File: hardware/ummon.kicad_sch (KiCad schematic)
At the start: 84 parts, among them J1 Conn_01x08_Pin, J2 Conn_01x05_Pin, J3 Conn_01x04_Pin, J4 Conn_01x04_Pin, J5 Conn_01x04_Pin, P1 FPC 0.5MM 24P Vertical, Q1 SI1308EDL, SW1 Reboot, SW2 Flash, SW3 Test Button, U1 ESP32-C6-WROOM-1-N8, U2 SCD41-D-R2, U3 SGP41-D-R4, U4 SHT41-AD1B-R2, U5 AMS1117-3.3

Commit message: :sparkles: Add various testpoints
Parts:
- added TP1, TP10, TP2, TP3, TP4, TP5, TP6, TP7, TP8, TP9: TestPoint, TestPoint:TestPoint_Pad_D1.0mm, symbol Connector:TestPoint
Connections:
- net +3.3V: now also TP10.1
- net +5V: now also TP8.1
- net EN: now also TP1.1
- net EPD_PREVGH: now also TP4.1
- net EPD_PREVGL: now also TP5.1
- net EPD_RESE: now also TP3.1
- net GND: now also TP9.1
- net GPIO9: now also TP2.1
- net EPD_VGL: now reaches C26.1, D3.2 (A), D4.1 (K)
- net EPD_VGL: now also TP6.1
- net EPD_VGH: now reaches C26.2, D2.2 (A), L1.2, Q1.3 (D)
- net EPD_VGH: now also TP7.1

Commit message: :construction: WIP buck converter
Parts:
- added L2: FTC252012S2R2MBCA, parts:IND-SMD_L2.5-W2.0_MHCHL2520, symbol parts:FTC252012S2R2MBCA
- added R17: 100kΩ, Resistor_SMD:R_0805_2012Metric, symbol Device:R_Small
- added R18: 49.9kΩ, Resistor_SMD:R_0805_2012Metric, symbol Device:R_Small
- added U6: TLV62569DBVR, parts:SOT-23-5_L3.0-W1.7-P0.95-LS2.8-BR, symbol parts:TLV62569DBVR
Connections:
- net +3.3V: now also R17.2, R18.1, U6.5 (FB); no longer C16.1, U5.4 (VOUT)
- net +5V: now also U6.1 (EN)
- net GND: now also R18.2, U6.2 (GND)
- new net: L2.1, U6.3 (SW)
- new net: L2.2, R17.1
- new net: C16.1, U5.4 (VOUT)
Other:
- moved on the sheet: C14, C15, C16, C17, LED1, R14, U5

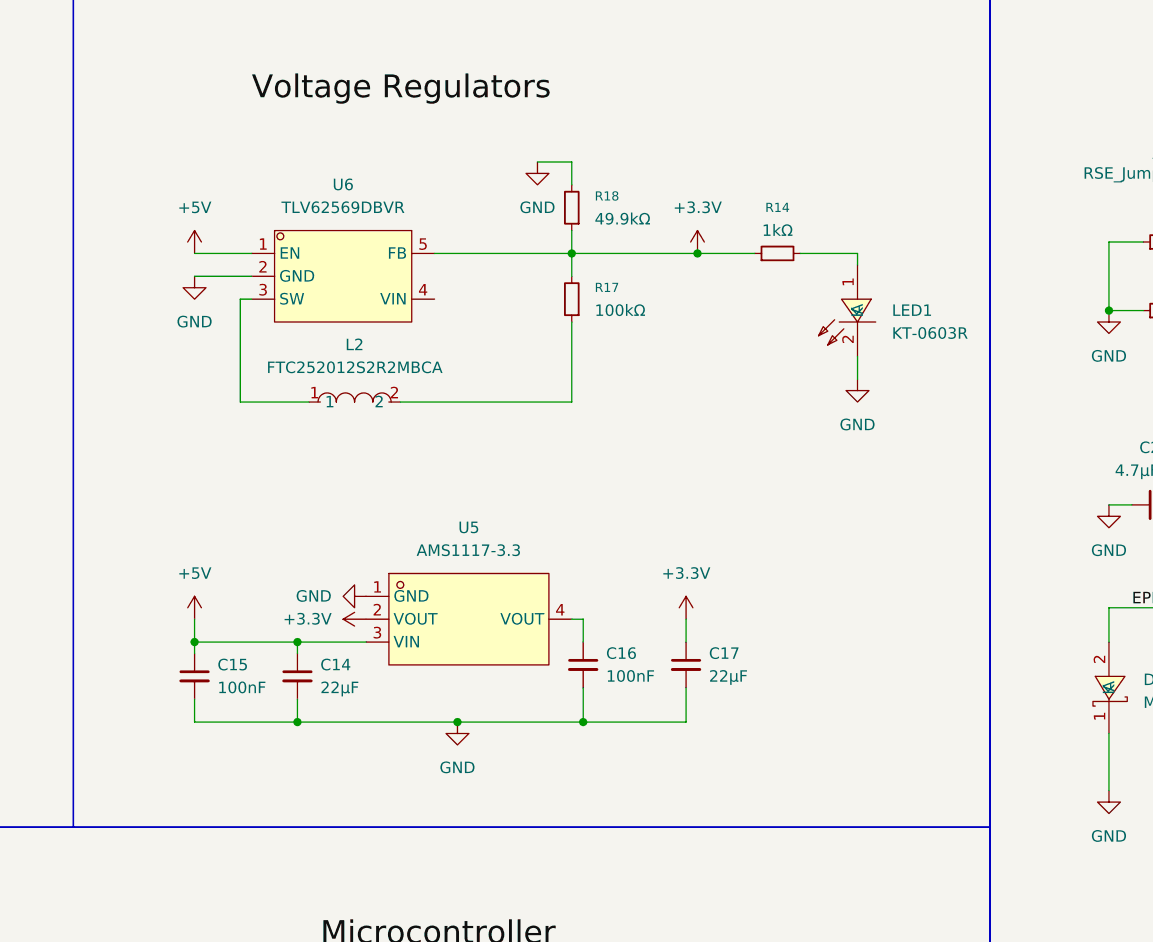
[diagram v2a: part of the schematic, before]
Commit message: Revert ":construction: WIP buck converter"
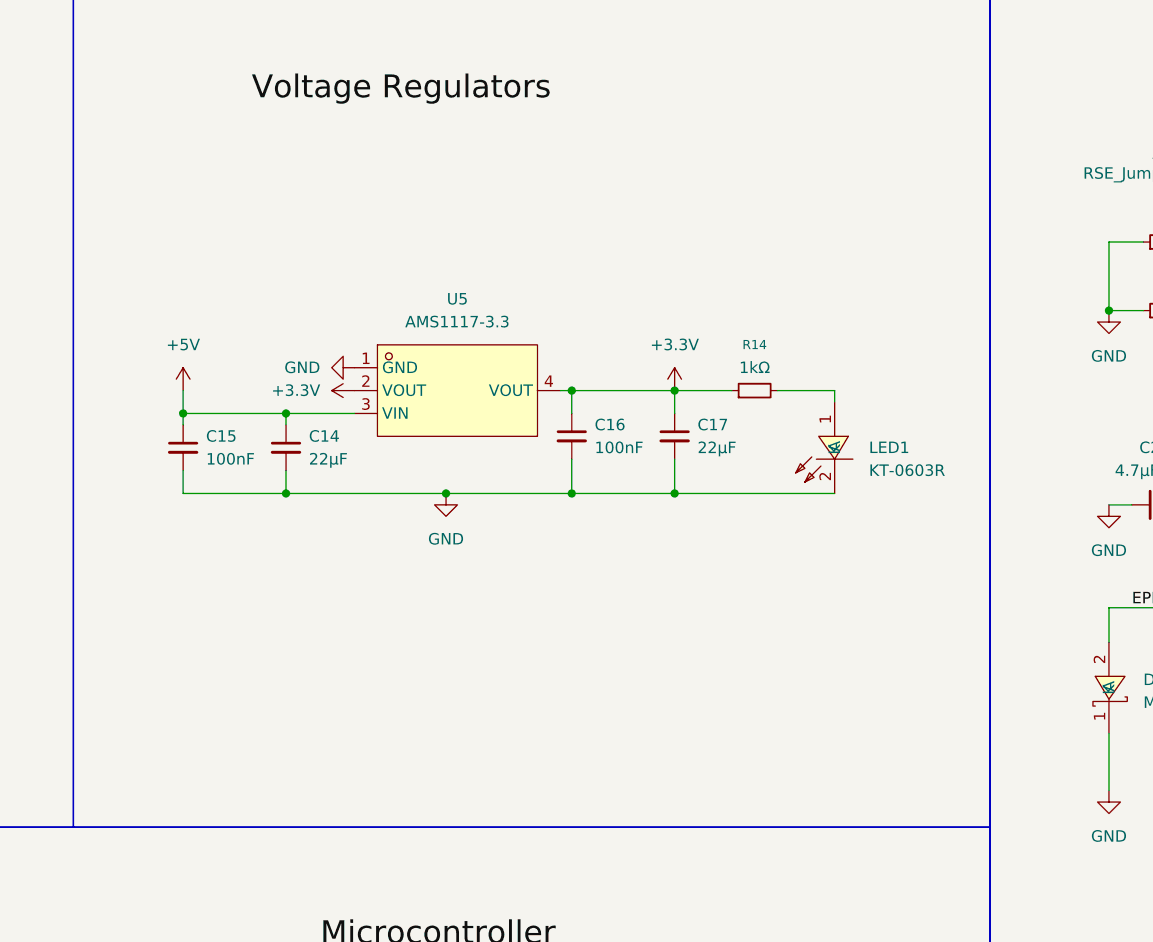
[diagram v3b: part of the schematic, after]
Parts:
- removed L2: FTC252012S2R2MBCA, parts:IND-SMD_L2.5-W2.0_MHCHL2520, symbol parts:FTC252012S2R2MBCA
- removed R17: 100kΩ, Resistor_SMD:R_0805_2012Metric, symbol Device:R_Small
- removed R18: 49.9kΩ, Resistor_SMD:R_0805_2012Metric, symbol Device:R_Small
- removed U6: TLV62569DBVR, parts:SOT-23-5_L3.0-W1.7-P0.95-LS2.8-BR, symbol parts:TLV62569DBVR
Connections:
- net +3.3V: now also C16.1, U5.4 (VOUT)
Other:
- moved on the sheet: C14, C15, C16, C17, LED1, R14, U5

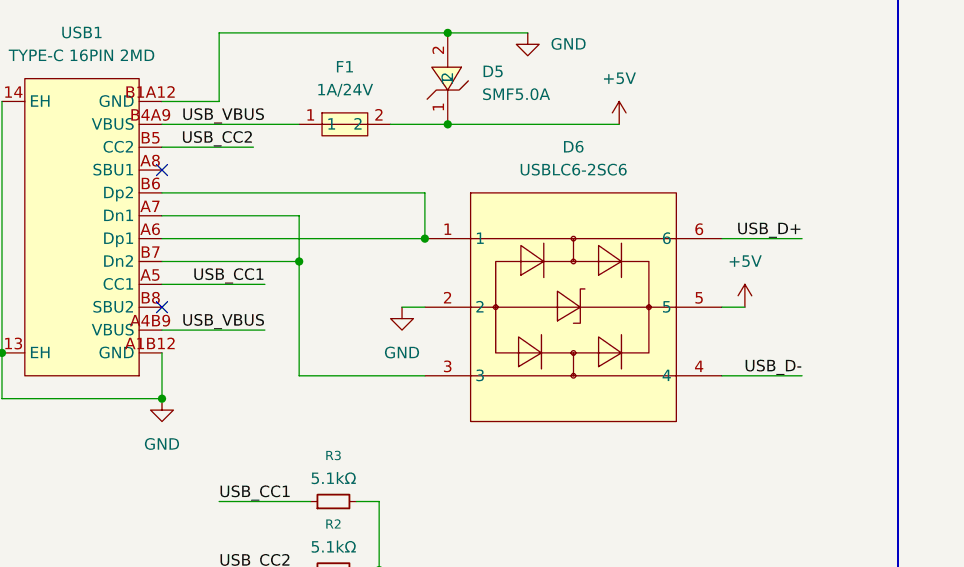
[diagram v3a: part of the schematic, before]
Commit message: :recycle: Swap USB data lines between USBLC6 channels
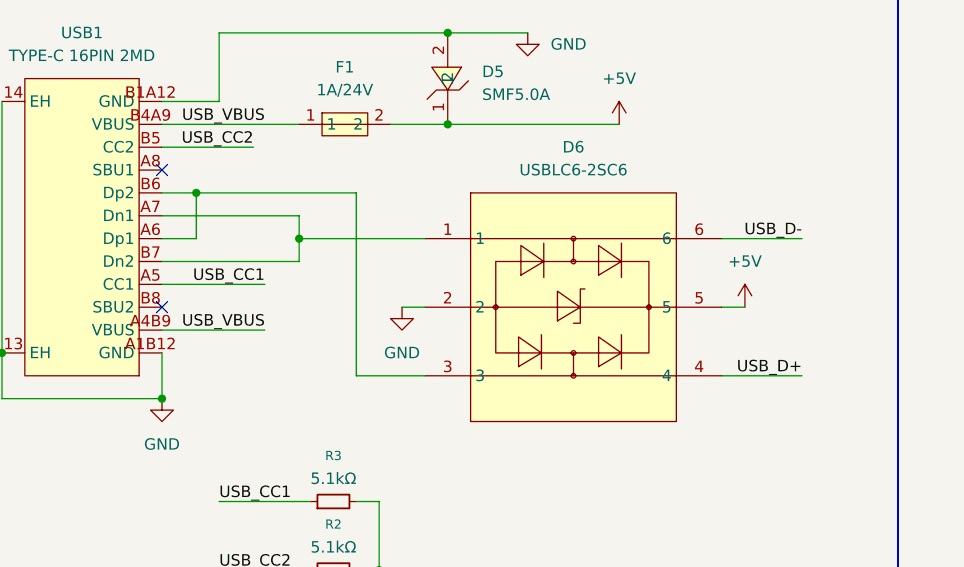
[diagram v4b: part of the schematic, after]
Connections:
- net USB_D+: now also D6.4; no longer D6.6
- net USB_D-: now also D6.6; no longer D6.4
- net at USB1.A6 (Dp1), USB1.B6 (Dp2): now also D6.3; no longer D6.1
- net at USB1.A7 (Dn1), USB1.B7 (Dn2): now also D6.1; no longer D6.3
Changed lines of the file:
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@@
 	)
 	(junction
-		(at 66.04 54.61)
+		(at 40.64 49.53)
 		(diameter 0)
 		(color 0 0 0 0)
@@
 	)
 	(junction
-		(at 52.07 57.15)
-		(diameter 0)
-		(color 0 0 0 0)
-	)
-	(junction
 		(at 364.49 83.82)
 		(diameter 0)
@@
 	)
 	(junction
+		(at 52.07 54.61)
+		(diameter 0)
+		(color 0 0 0 0)
+	)
+	(junction
 		(at 67.31 152.4)
 		(diameter 0)
@@
 	(wire
 		(pts
-			(xy 52.07 57.15) (xy 52.07 52.07)
+			(xy 52.07 57.15) (xy 52.07 54.61)
 		)
 		(stroke
@@
 	(wire
 		(pts
+			(xy 40.64 54.61) (xy 40.64 49.53)
+		)
+		(stroke
+			(width 0)
+			(type default)
+		)
+	)
+	(wire
+		(pts
 			(xy 227.33 248.92) (xy 227.33 255.27)
 		)
@@
 	(wire
 		(pts
-			(xy 203.2 55.88) (xy 203.2 57.15)
+			(xy 52.07 54.61) (xy 52.07 52.07)
 		)
 		(stroke
@@
 	(wire
 		(pts
-			(xy 134.62 134.62) (xy 134.62 133.35)
+			(xy 203.2 55.88) (xy 203.2 57.15)
 		)
 		(stroke
@@
 	(wire
 		(pts
-			(xy 227.33 243.84) (xy 227.33 237.49)
+			(xy 134.62 134.62) (xy 134.62 133.35)
 		)
 		(stroke
@@
 	(wire
 		(pts
-			(xy 17.78 173.99) (xy 24.13 173.99)
+			(xy 227.33 243.84) (xy 227.33 237.49)
 		)
 		(stroke
@@
 	(wire
 		(pts
-			(xy 247.65 237.49) (xy 271.78 237.49)
+			(xy 17.78 173.99) (xy 24.13 173.99)
 		)
 		(stroke
@@
 	(wire
 		(pts
-			(xy 270.51 80.01) (xy 270.51 83.82)
+			(xy 247.65 237.49) (xy 271.78 237.49)
 		)
 		(stroke
@@
 	(wire
 		(pts
-			(xy 66.04 49.53) (xy 66.04 54.61)
+			(xy 270.51 80.01) (xy 270.51 83.82)
 		)
 		(stroke
@@
 	(wire
 		(pts
-			(xy 52.07 69.85) (xy 66.04 69.85)
-		)
-		(stroke
-			(width 0)
-			(type default)
-		)
-	)
-	(wire
-		(pts
 			(xy 370.84 40.64) (xy 382.27 40.64)
 		)
@@
 	(wire
 		(pts
-			(xy 365.76 67.31) (xy 365.76 71.12)
+			(xy 36.83 54.61) (xy 40.64 54.61)
 		)
 		(stroke
@@
 	(wire
 		(pts
-			(xy 22.86 137.16) (xy 29.21 137.16)
+			(xy 365.76 67.31) (xy 365.76 71.12)
 		)
 		(stroke
@@
 	(wire
 		(pts
-			(xy 248.92 107.95) (xy 251.46 107.95)
+			(xy 22.86 137.16) (xy 29.21 137.16)
 		)
 		(stroke
@@
 	(wire
 		(pts
-			(xy 173.99 55.88) (xy 172.72 55.88)
+			(xy 248.92 107.95) (xy 251.46 107.95)
 		)
 		(stroke
@@
 	(wire
 		(pts
-			(xy 138.43 166.37) (xy 133.35 166.37)
+			(xy 173.99 55.88) (xy 172.72 55.88)
 		)
 		(stroke
@@
 	(wire
 		(pts
-			(xy 196.85 55.88) (xy 203.2 55.88)
+			(xy 138.43 166.37) (xy 133.35 166.37)
 		)
 		(stroke
@@
 	(wire
 		(pts
-			(xy 36.83 49.53) (xy 66.04 49.53)
+			(xy 196.85 55.88) (xy 203.2 55.88)
 		)
 		(stroke
@@
 	(wire
 		(pts
+			(xy 58.42 69.85) (xy 66.04 69.85)
+		)
+		(stroke
+			(width 0)
+			(type default)
+		)
+	)
+	(wire
+		(pts
 			(xy 207.01 237.49) (xy 213.36 237.49)
 		)
@@
 	(wire
 		(pts
+			(xy 40.64 49.53) (xy 58.42 49.53)
+		)
+		(stroke
+			(width 0)
+			(type default)
+		)
+	)
+	(wire
+		(pts
 			(xy 46.99 173.99) (xy 35.56 173.99)
 		)
@@
 	(wire
 		(pts
+			(xy 52.07 54.61) (xy 66.04 54.61)
+		)
+		(stroke
+			(width 0)
+			(type default)
+		)
+	)
+	(wire
+		(pts
 			(xy 68.58 41.91) (xy 87.63 41.91)
 		)
@@
 	(wire
 		(pts
-			(xy 36.83 54.61) (xy 66.04 54.61)
-		)
-		(stroke
-			(width 0)
-			(type default)
-		)
-	)
-	(wire
-		(pts
 			(xy 130.81 59.69) (xy 130.81 58.42)
 		)
@@
 	(wire
 		(pts
+			(xy 58.42 49.53) (xy 58.42 69.85)
+		)
+		(stroke
+			(width 0)
+			(type default)
+		)
+	)
+	(wire
+		(pts
 			(xy 247.65 259.08) (xy 251.46 259.08)
 		)
@@
 	(wire
 		(pts
+			(xy 36.83 49.53) (xy 40.64 49.53)
+		)
+		(stroke
+			(width 0)
+			(type default)
+		)
+	)
+	(wire
+		(pts
 			(xy 353.06 93.98) (xy 382.27 93.98)
 		)
@@
 	(wire
 		(pts
-			(xy 52.07 57.15) (xy 52.07 69.85)
-		)
-		(stroke
-			(width 0)
-			(type default)
-		)
-	)
-	(wire
-		(pts
 			(xy 149.86 240.03) (xy 149.86 241.3)
 		)
@@
 		)
 	)
-	(label "USB_D+"
-		(at 107.95 54.61 180)
-		(effects
-			(font
-				(size 1.27 1.27)
-			)
-			(justify right bottom)
-		)
-	)
 	(label "I2C_SCL"
 		(at 389.89 185.42 180)
@@
 	)
 	(label "USB_D+"
+		(at 107.95 69.85 180)
+		(effects
+			(font
+				(size 1.27 1.27)
+			)
+			(justify right bottom)
+		)
+	)
+	(label "USB_D+"
 		(at 133.35 171.45 180)
 		(effects
@@
 		)
 	)
-	(label "USB_D-"
-		(at 107.95 69.85 180)
-		(effects
-			(font
-				(size 1.27 1.27)
-			)
-			(justify right bottom)
-		)
-	)
 	(label "USB_CC2"
 		(at 43.18 91.44 0)
@@
 		)
 	)
+	(label "USB_D-"
+		(at 107.95 54.61 180)
+		(effects
+			(font
+				(size 1.27 1.27)
+			)
+			(justify right bottom)
+		)
+	)

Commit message: :construction: WIP place ESD parts and route epd charge pump
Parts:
- added C18: 22µF, Capacitor_SMD:C_1206_3216Metric, symbol Device:C_Small
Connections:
- net +3.3V: now also C18.2
- net GND: now also C18.1
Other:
- moved on the sheet: C22
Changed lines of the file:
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@@
 	)
 	(junction
+		(at 229.87 46.99)
+		(diameter 0)
+		(color 0 0 0 0)
+	)
+	(junction
 		(at 149.86 247.65)
 		(diameter 0)
@@
 	)
 	(junction
+		(at 229.87 68.58)
+		(diameter 0)
+		(color 0 0 0 0)
+	)
+	(junction
 		(at 160.02 133.35)
 		(diameter 0)
@@
 	)
 	(junction
-		(at 233.68 46.99)
-		(diameter 0)
-		(color 0 0 0 0)
-	)
-	(junction
 		(at 342.9 93.98)
 		(diameter 0)
@@
 	)
 	(junction
+		(at 242.57 68.58)
+		(diameter 0)
+		(color 0 0 0 0)
+	)
+	(junction
 		(at 217.17 237.49)
 		(diameter 0)
@@
 	(wire
 		(pts
+			(xy 238.76 58.42) (xy 242.57 58.42)
+		)
+		(stroke
+			(width 0)
+			(type default)
+		)
+	)
+	(wire
+		(pts
 			(xy 342.9 86.36) (xy 342.9 88.9)
 		)
@@
 	(wire
 		(pts
+			(xy 229.87 68.58) (xy 233.68 68.58)
+		)
+		(stroke
+			(width 0)
+			(type default)
+		)
+	)
+	(wire
+		(pts
 			(xy 60.96 142.24) (xy 60.96 152.4)
 		)
@@
 	(wire
 		(pts
+			(xy 242.57 58.42) (xy 242.57 68.58)
+		)
+		(stroke
+			(width 0)
+			(type default)
+		)
+	)
+	(wire
+		(pts
 			(xy 342.9 93.98) (xy 342.9 97.79)
 		)
@@
 	(wire
 		(pts
-			(xy 233.68 46.99) (xy 237.49 46.99)
-		)
-		(stroke
-			(width 0)
-			(type default)
-		)
-	)
-	(wire
-		(pts
 			(xy 270.51 62.23) (xy 270.51 64.77)
 		)
@@
 	(wire
 		(pts
-			(xy 237.49 39.37) (xy 233.68 39.37)
+			(xy 237.49 39.37) (xy 229.87 39.37)
 		)
 		(stroke
@@
 	(wire
 		(pts
+			(xy 229.87 46.99) (xy 237.49 46.99)
+		)
+		(stroke
+			(width 0)
+			(type default)
+		)
+	)
+	(wire
+		(pts
 			(xy 146.05 247.65) (xy 149.86 247.65)
 		)
@@
 	(wire
 		(pts
+			(xy 229.87 58.42) (xy 229.87 68.58)
+		)
+		(stroke
+			(width 0)
+			(type default)
+		)
+	)
+	(wire
+		(pts
 			(xy 217.17 248.92) (xy 224.79 248.92)
 		)
@@
 	(wire
 		(pts
+			(xy 242.57 68.58) (xy 246.38 68.58)
+		)
+		(stroke
+			(width 0)
+			(type default)
+		)
+	)
+	(wire
+		(pts
 			(xy 39.37 255.27) (xy 52.07 255.27)
 		)
@@
 	(wire
 		(pts
-			(xy 241.3 68.58) (xy 246.38 68.58)
+			(xy 238.76 68.58) (xy 242.57 68.58)
 		)
 		(stroke
@@
 	(wire
 		(pts
-			(xy 233.68 39.37) (xy 233.68 46.99)
+			(xy 229.87 39.37) (xy 229.87 46.99)
 		)
 		(stroke
@@
 	(wire
 		(pts
-			(xy 233.68 68.58) (xy 236.22 68.58)
-		)
-		(stroke
-			(width 0)
-			(type default)
-		)
-	)
-	(wire
-		(pts
 			(xy 67.31 130.81) (xy 78.74 130.81)
 		)
@@
 	(wire
 		(pts
+			(xy 233.68 58.42) (xy 229.87 58.42)
+		)
+		(stroke
+			(width 0)
+			(type default)
+		)
+	)
+	(wire
+		(pts
 			(xy 307.34 227.33) (xy 320.04 227.33)
 		)
@@
 	(symbol
 		(lib_id "power:GND")
-		(at 233.68 46.99 0)
+		(at 229.87 46.99 0)
 		(unit 1)
 		(body_style 1)
@@
 		(fields_autoplaced yes)
 		(property "Reference" "#PWR043"
-			(at 233.68 53.34 0)
+			(at 229.87 53.34 0)
 			(hide yes)
 			(show_name no)
@@
 		)
 		(property "Value" "GND"
-			(at 233.68 52.07 0)
+			(at 229.87 52.07 0)
 			(show_name no)
 			(do_not_autoplace no)
@@
 		)
 		(property "Footprint" ""
-			(at 233.68 46.99 0)
+			(at 229.87 46.99 0)
 			(hide yes)
 			(show_name no)
@@
 		)
 		(property "Datasheet" ""
-			(at 233.68 46.99 0)
+			(at 229.87 46.99 0)
 			(hide yes)
 			(show_name no)
@@
 		)
 		(property "Description" "Power symbol creates a global label with name \"GND\" , ground"
-			(at 233.68 46.99 0)
+			(at 229.87 46.99 0)
 			(hide yes)
 			(show_name no)
@@
 	(symbol
 		(lib_id "Device:C_Small")
+		(at 236.22 58.42 90)
+		(unit 1)
+		(body_style 1)
+		(exclude_from_sim no)
+		(in_bom yes)
+		(on_board yes)
+		(in_pos_files yes)
+		(dnp no)
+		(fields_autoplaced yes)
+		(property "Reference" "C18"
+			(at 236.2263 52.07 90)
+			(show_name no)
+			(do_not_autoplace no)
+			(effects
+				(font
+					(size 1.27 1.27)
+				)
+			)
+		)
+		(property "Value" "22µF"
+			(at 236.2263 54.61 90)
+			(show_name no)
+			(do_not_autoplace no)
+			(effects
+				(font
+					(size 1.27 1.27)
+				)
+			)
+		)
+		(property "Footprint" "Capacitor_SMD:C_1206_3216Metric"
+			(at 236.22 58.42 0)
+			(hide yes)
+			(show_name no)
+			(do_not_autoplace no)
+			(effects
+				(font
+					(size 1.27 1.27)
+				)
+			)
+		)
+		(property "Datasheet" ""
+			(at 236.22 58.42 0)
+			(hide yes)
+			(show_name no)
+			(do_not_autoplace no)
+			(effects
+				(font
+					(size 1.27 1.27)
+				)
+			)
+		)
+		(property "Description" "Unpolarized capacitor, small symbol"
+			(at 236.22 58.42 0)
+			(hide yes)
+			(show_name no)
+			(do_not_autoplace no)
+			(effects
+				(font
+					(size 1.27 1.27)
+				)
+			)
+		)
+		(property "LCSC Part" "C12891"
+			(at 236.22 58.42 0)
+			(hide yes)
+			(show_name no)
+			(do_not_autoplace no)
+			(effects
+				(font
+					(size 1.27 1.27)
+				)
+			)
+		)
+		(pin "1"
+		)
+		(pin "2"
+		)
+		(instances
+			(project "ummon"
+				(path "/535d19c6-6731-456b-b7fb-ac6bb0b86499"
+					(reference "C18")
+					(unit 1)
+				)
+			)
+		)
+	)
+	(symbol
+		(lib_id "Device:C_Small")
 		(at 350.52 67.31 90)
 		(unit 1)
@@
 	(symbol
 		(lib_id "power:GND")
-		(at 233.68 68.58 0)
+		(at 229.87 68.58 0)
 		(unit 1)
 		(body_style 1)
@@
 		(fields_autoplaced yes)
 		(property "Reference" "#PWR044"
-			(at 233.68 74.93 0)
+			(at 229.87 74.93 0)
 			(hide yes)
 			(show_name no)
@@
 		)
 		(property "Value" "GND"
-			(at 233.68 73.66 0)
+			(at 229.87 73.66 0)
 			(show_name no)
 			(do_not_autoplace no)
@@
 		)
 		(property "Footprint" ""
-			(at 233.68 68.58 0)
+			(at 229.87 68.58 0)
 			(hide yes)
 			(show_name no)
@@
 		)
 		(property "Datasheet" ""
-			(at 233.68 68.58 0)
+			(at 229.87 68.58 0)
 			(hide yes)
 			(show_name no)
@@
 		)
 		(property "Description" "Power symbol creates a global label with name \"GND\" , ground"
-			(at 233.68 68.58 0)
+			(at 229.87 68.58 0)
 			(hide yes)
 			(show_name no)
@@
 	(symbol
 		(lib_id "Device:C_Small")
-		(at 238.76 68.58 90)
+		(at 236.22 68.58 90)
 		(unit 1)
 		(body_style 1)
@@
 		(fields_autoplaced yes)
 		(property "Reference" "C22"
-			(at 238.7663 62.23 90)
+			(at 236.2263 62.23 90)
 			(show_name no)
 			(do_not_autoplace no)
@@
 		)
 		(property "Value" "4.7μF/50V"
-			(at 238.7663 64.77 90)
+			(at 236.2263 64.77 90)
 			(show_name no)
 			(do_not_autoplace no)
@@
 		)
 		(property "Footprint" "Capacitor_SMD:C_1206_3216Metric"
-			(at 238.76 68.58 0)
+			(at 236.22 68.58 0)
 			(hide yes)
 			(show_name no)
@@
 		)
 		(property "Datasheet" ""
-			(at 238.76 68.58 0)
+			(at 236.22 68.58 0)
 			(hide yes)
 			(show_name no)
@@
 		)
 		(property "Description" "Unpolarized capacitor, small symbol"
-			(at 238.76 68.58 0)
+			(at 236.22 68.58 0)
 			(hide yes)
 			(show_name no)
@@
 		)
 		(property "LCSC Part" "C29823"
-			(at 238.76 68.58 90)
+			(at 236.22 68.58 90)
 			(hide yes)
 			(show_name no)

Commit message: :construction: WIP name USB port data nets and unplace ldo
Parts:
- renumbered TP2 to TP10, TP10 to TP2
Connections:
- net USB_PORT_D+: now reaches D6.1, USB1.A7 (Dn1), USB1.B7 (Dn2)
- net USB_PORT_D-: now reaches D6.3, USB1.A6 (Dp1), USB1.B6 (Dp2)
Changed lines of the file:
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@@
 		)
 	)
+	(label "USB_PORT_D+"
+		(at 52.07 57.15 180)
+		(effects
+			(font
+				(size 1.27 1.27)
+			)
+			(justify right bottom)
+		)
+	)
 	(label "H_PRESENCE"
 		(at 323.85 189.23 0)
@@
 		)
 	)
+	(label "USB_PORT_D-"
+		(at 55.88 49.53 180)
+		(effects
+			(font
+				(size 1.27 1.27)
+			)
+			(justify right bottom)
+		)
+	)
 	(label "RX"
 		(at 360.68 180.34 180)
@@
 		(dnp no)
 		(fields_autoplaced yes)
-		(property "Reference" "TP2"
+		(property "Reference" "TP10"
 			(at 309.88 220.2179 0)
 			(show_name no)
@@
 			(project "ummon"
 				(path "/535d19c6-6731-456b-b7fb-ac6bb0b86499"
-					(reference "TP2")
+					(reference "TP10")
 					(unit 1)
 				)
@@
 		(dnp no)
 		(fields_autoplaced yes)
-		(property "Reference" "TP10"
+		(property "Reference" "TP2"
 			(at 347.98 240.5379 0)
 			(show_name no)
@@
 			(project "ummon"
 				(path "/535d19c6-6731-456b-b7fb-ac6bb0b86499"
-					(reference "TP10")
+					(reference "TP2")
 					(unit 1)
 				)
